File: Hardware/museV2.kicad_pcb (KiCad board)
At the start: 2 copper layers, 276 parts, among them P1 RCA_conn_x2, P10 -15V, P11 ~3, P13 ~4, P14 +5V, P18 RX1, P19 3.3V, P2 +12V, P20 TX2, P21 1.8V, P22 PSU_CTL, P23 GND, P27 D1, P29 D2, P3 3.5mm_conn_tip_switch, P30 D3, P31 P1, P32 L1.8_1, P33 L3.3_1, P34 P2, P35 L1.8_2, P36 L3.3_2, P37 P3, P38 L1.8_3, P39 L3.3_3, P4 3.5mm_conn_tip_switch, P40 P4, P41 L1.8_4, P42 L3.3_4, P43 +5V, P44 +12V_AUX, P45 +5V_AUX, P5 CONN_01X06, P6 CONN_02X14, P7 ~5, P8 +15V, P9 ~6, Q1 PMOS, Q2 BSS138, SW1 PWR_BTN, SW2 PWR_BTN, U1 TPS65130, U10 PCM1863, U11 PCM1796, U12 NE5534, U13 NE5534, U14 NE5534, U15 NE5534, U16 NE5534, U17 NE5534, U18 EdisonConnector, U19 GTL2010, U2 LP38692, U20 GTL2010, U21 GTL2010, U22 PCA9685BS, U3 PLR135/T10, U4 POM-3535L-3-R, U5 POM-3535L-3-R, U6 PLT133/T10W, U7 POM-3535L-3-R, U8 POM-3535L-3-R, U9 PCM9211, X1 24.576 MHz

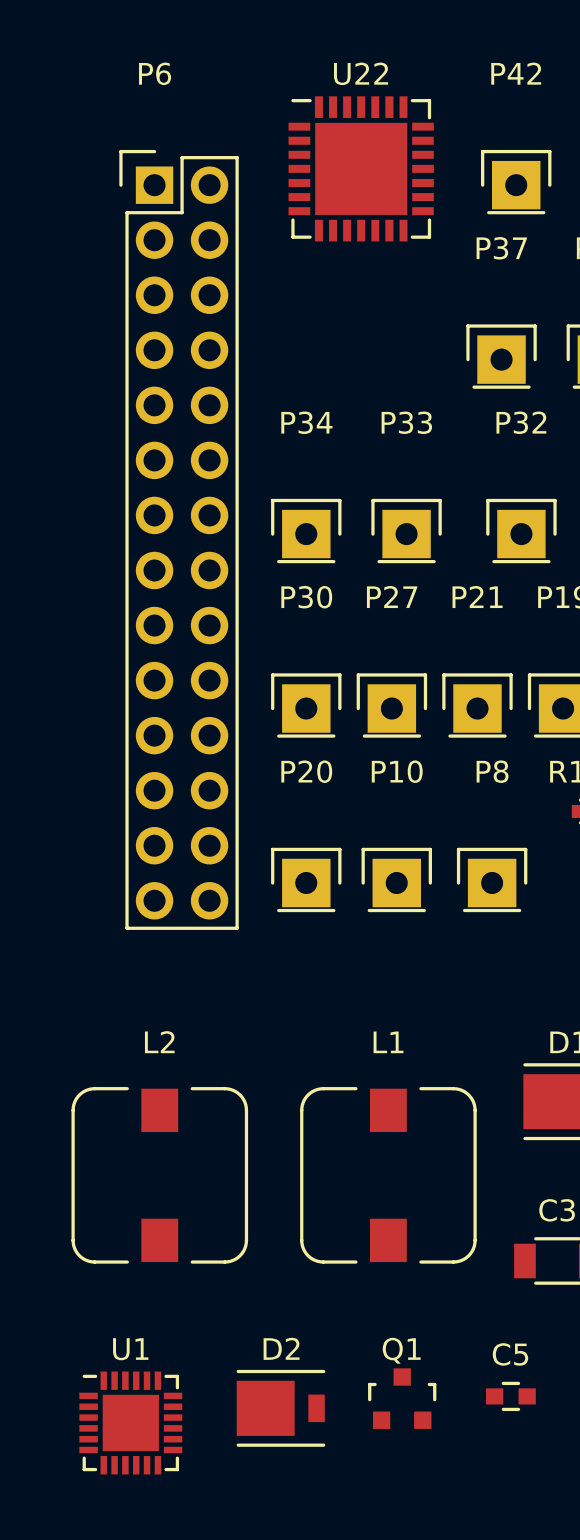
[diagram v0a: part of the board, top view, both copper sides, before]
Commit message: Updated QFN footprints with thermal evacuation vias
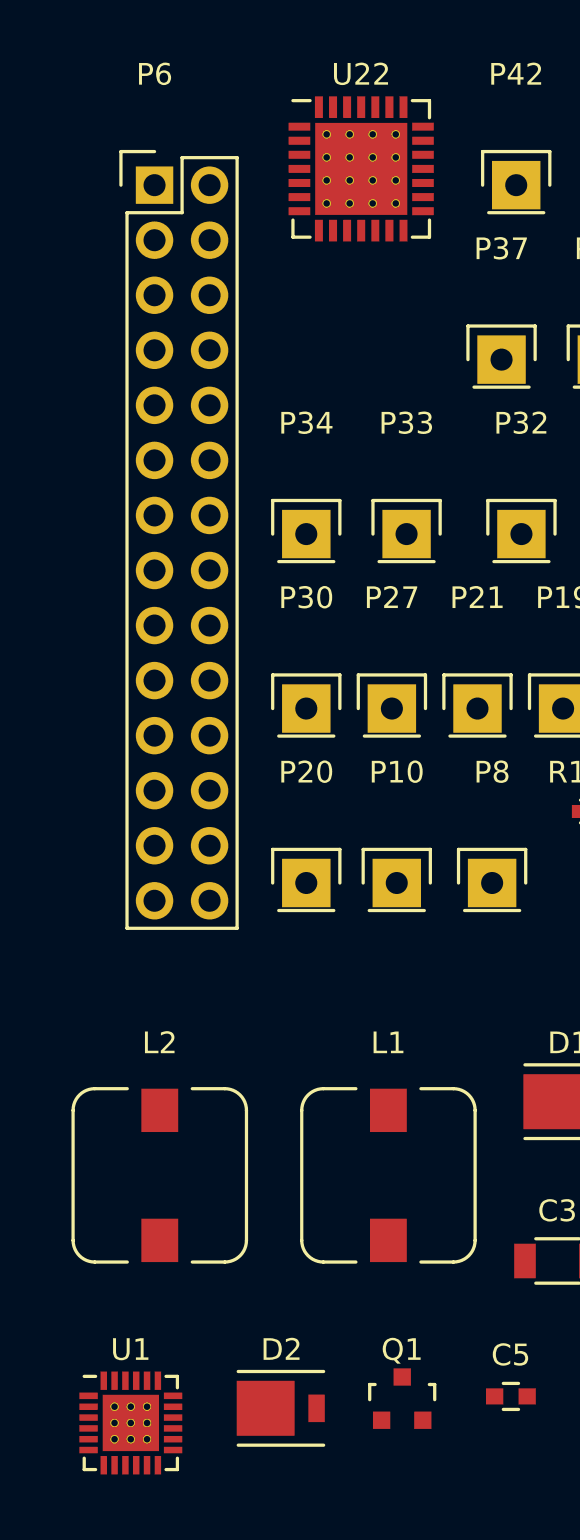
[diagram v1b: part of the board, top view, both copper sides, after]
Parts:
- U1: footprint Housings_DFN_QFN:QFN-24-1EP_4x4mm_Pitch0.5mm -> muse-v2-lib:QFN-24-1EP_4x4mm_Pitch0.5mm_THERMAL
- U22: footprint Housings_DFN_QFN:QFN-28-1EP_6x6mm_Pitch0.65mm -> muse-v2-lib:QFN-28-1EP_6x6mm_Pitch0.65mm_THERMAL

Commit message: Routing split rail DC/DC converter
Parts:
- added REF**: VIA-0.3mm, muse-v2-lib:VIA-0.3mm, F.Cu at (45.4, 151.9)
- added REF**: VIA-0.3mm, muse-v2-lib:VIA-0.3mm, F.Cu at (44.7, 151.9)
- moved C7 53.4 mm to (48.7, 156.6), turned to 270 degrees
- moved C6 51.9 mm to (44.0, 154.0), turned to 180 degrees
- moved C2 49.6 mm to (47.2, 146.5)
- moved R1 48.7 mm to (47.3, 147.8), turned to 180 degrees
- moved R5 44.1 mm to (46.9, 155.8), turned to 180 degrees
- moved R4 41.3 mm to (52.4, 152.6), turned to 180 degrees
- moved D1 40.6 mm to (43.7, 149.0), turned to 270 degrees
- moved C10 39.9 mm to (53.7, 154.4)
- moved C4 39.7 mm to (52.8, 149.5)
- moved C1 38.5 mm to (42.9, 152.4)
- moved L1 38.4 mm to (36.4, 150.7), turned to 90 degrees
- moved R3 38.3 mm to (47.3, 149.1)
- moved R2 37.9 mm to (52.4, 151.1)
- moved C9 35.9 mm to (50.6, 147.7), turned to 90 degrees
- moved C8 34.2 mm to (49.1, 147.7), turned to 90 degrees
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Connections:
- U1 pad 25: (no net) -> GND
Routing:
- added copper zone on F.Cu, net -15V
- added copper zone on F.Cu, net GND
- added copper zone on F.Cu, net Net-(C4-Pad1)
- added copper zone on F.Cu, net Net-(C5-Pad1)
- added copper zone on F.Cu, net Net-(D2-Pad1)
